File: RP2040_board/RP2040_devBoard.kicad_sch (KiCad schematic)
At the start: 14 parts, among them U1 RP2040

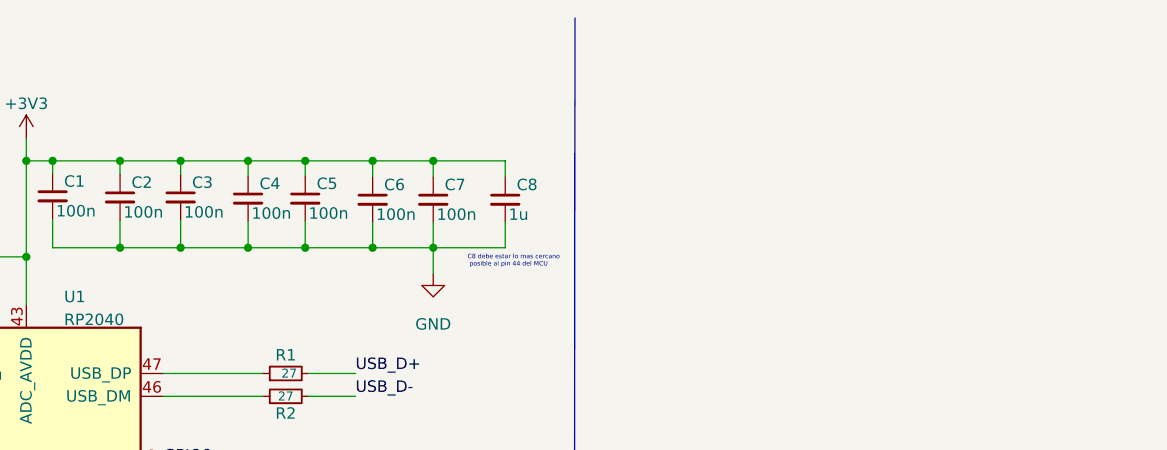
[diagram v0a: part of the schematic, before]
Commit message: ESCH: added the schematic of the power supply and did the wiring
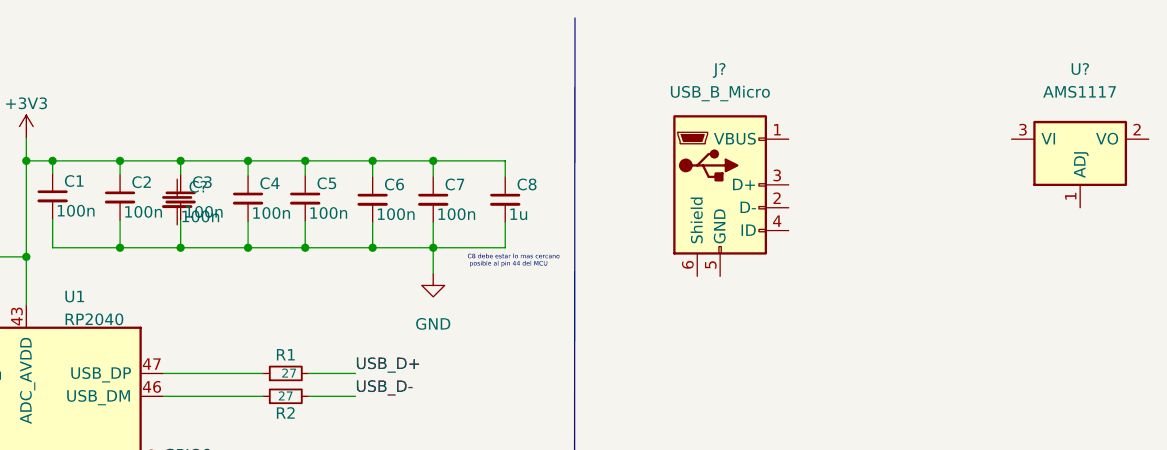
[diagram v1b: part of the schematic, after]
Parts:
- added C?: 100n, symbol Device:C_Small
- added J?: USB_B_Micro, symbol Connector:USB_B_Micro
- added U?: AMS1117, Package_TO_SOT_SMD:SOT-223-3_TabPin2, symbol Regulator_Linear:AMS1117
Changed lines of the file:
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@@
     (pin "2")
+  )
+  (symbol (lib_id "Connector:USB_B_Micro") (at 155.829 30.607 0) (unit 1)
+    (in_bom yes) (on_board yes) (fields_autoplaced)
+    (property "Reference" "J?" (id 0) (at 155.829 17.78 0))
+    (property "Value" "USB_B_Micro" (id 1) (at 155.829 20.32 0))
+    (property "Footprint" "" (id 2) (at 159.639 31.877 0)
+      (effects (font (size 1.27 1.27)) hide)
+    )
+    (property "Datasheet" "~" (id 3) (at 159.639 31.877 0)
+      (effects (font (size 1.27 1.27)) hide)
+    )
+    (pin "1")
+    (pin "2")
+    (pin "3")
+    (pin "4")
+    (pin "5")
+    (pin "6")
   )
   (symbol (lib_id "power:GND") (at 123.952 40.513 0) (unit 1)
@@
     (pin "1")
     (pin "2")
+  )
+  (symbol (lib_id "Device:C_Small") (at 95.504 32.512 0) (unit 1)
+    (in_bom yes) (on_board yes)
+    (property "Reference" "C?" (id 0) (at 96.774 30.861 0)
+      (effects (font (size 1.27 1.27)) (justify left))
+    )
+    (property "Value" "100n" (id 1) (at 95.885 34.163 0)
+      (effects (font (size 1.27 1.27)) (justify left))
+    )
+    (property "Footprint" "" (id 2) (at 95.504 32.512 0)
+      (effects (font (size 1.27 1.27)) hide)
+    )
+    (property "Datasheet" "~" (id 3) (at 95.504 32.512 0)
+      (effects (font (size 1.27 1.27)) hide)
+    )
+    (pin "1")
+    (pin "2")
+  )
+  (symbol (lib_id "Regulator_Linear:AMS1117") (at 195.834 25.527 0) (unit 1)
+    (in_bom yes) (on_board yes) (fields_autoplaced)
+    (property "Reference" "U?" (id 0) (at 195.834 17.78 0))
+    (property "Value" "AMS1117" (id 1) (at 195.834 20.32 0))
+    (property "Footprint" "Package_TO_SOT_SMD:SOT-223-3_TabPin2" (id 2) (at 195.834 20.447 0)
+      (effects (font (size 1.27 1.27)) hide)
+    )
+    (property "Datasheet" "http://www.advanced-monolithic.com/pdf/ds1117.pdf" (id 3) (at 198.374 31.877 0)
+      (effects (font (size 1.27 1.27)) hide)
+    )
+    (pin "1")
+    (pin "2")
+    (pin "3")
   )
   (symbol (lib_id "Device:C_Small") (at 117.221 32.258 0) (unit 1)
@@
       (reference "C11") (unit 1) (value "100n") (footprint "")
     )
+    (path "/c184ec07-2ca3-431a-b1d7-87c5d244f97c"
+      (reference "C?") (unit 1) (value "100n") (footprint "")
+    )
+    (path "/62979524-2b61-4177-baa6-d541cfcb37b3"
+      (reference "J?") (unit 1) (value "USB_B_Micro") (footprint "")
+    )
     (path "/ff75c5c2-f457-45cc-a1b3-0ec8763f2644"
       (reference "R1") (unit 1) (value "27 ") (footprint "")
@@
       (reference "U1") (unit 1) (value "RP2040") (footprint "RP2040_minimal:RP2040-QFN-56")
     )
-  )
+    (path "/c332c69c-d979-473f-ae67-7a4fc27098e4"
+      (reference "U?") (unit 1) (value "AMS1117") (footprint "Package_TO_SOT_SMD:SOT-223-3_TabPin2")
+    )
+  )

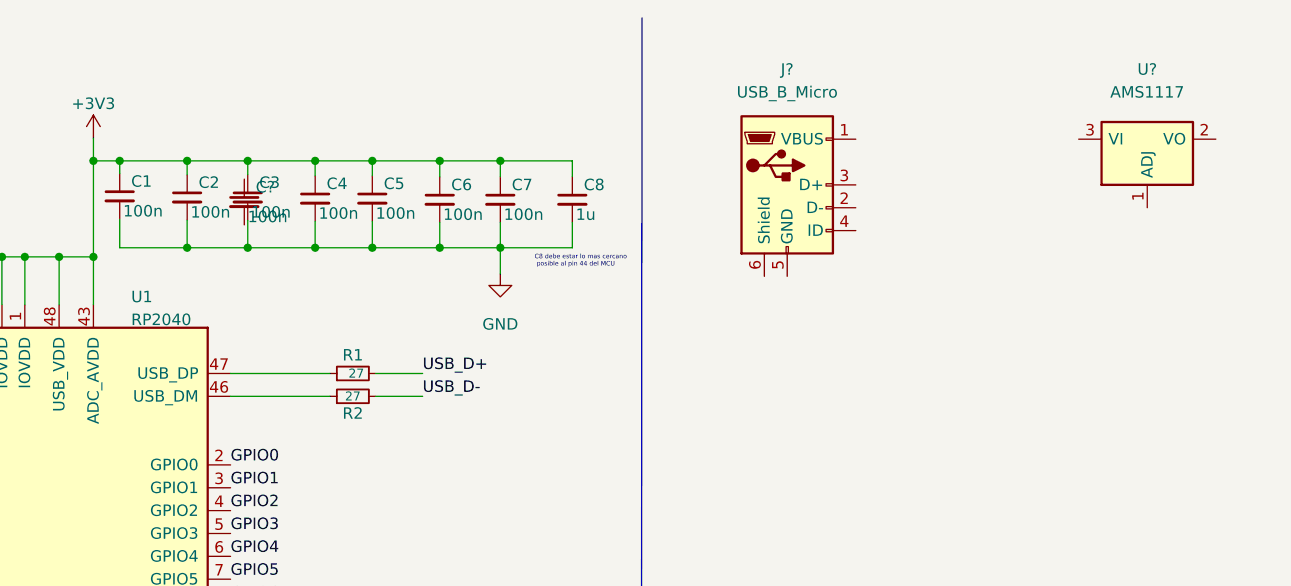
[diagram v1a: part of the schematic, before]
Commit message: sch: labeling of capacitor decoupling
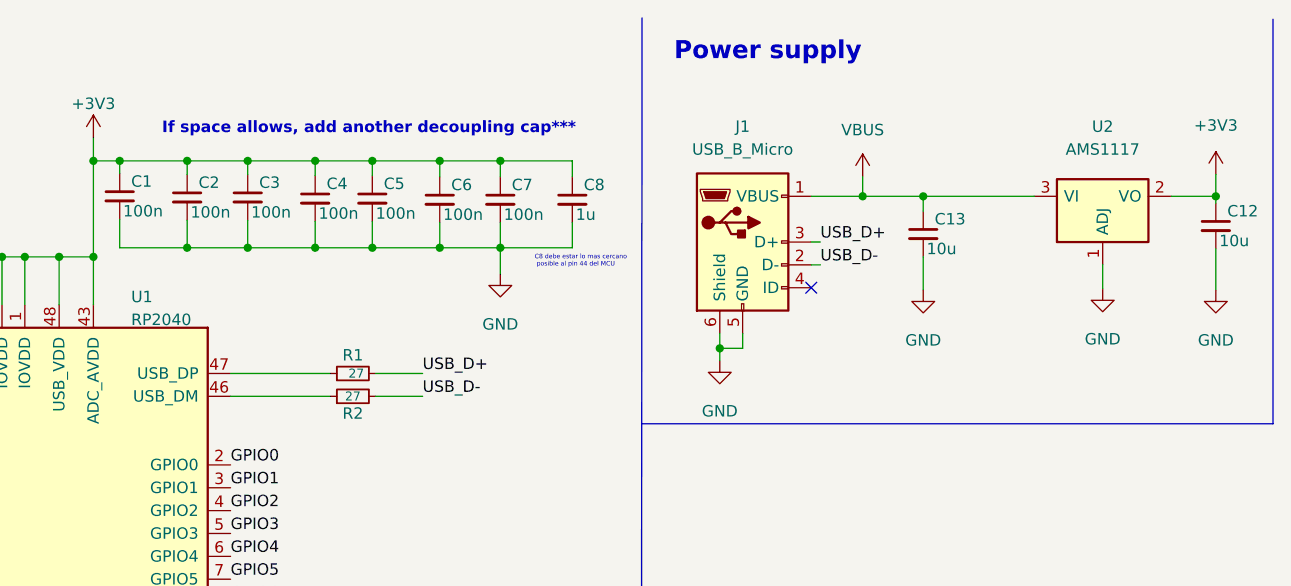
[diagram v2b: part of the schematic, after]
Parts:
- added C12: 10u, symbol Device:C_Small
- C13: renamed from C?; value 100n -> 10u
- gave numbers to parts that had none: 2
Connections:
- net +3V3: now also U2.2 (VO), C12.1
- net GND: now also C13.2, J1.5 (GND), J1.6 (Shield), U2.1 (ADJ), C12.2
- net USB_D+: now also J1.3 (D+)
- net USB_D-: now also J1.2 (D-)
- net VBUS: now reaches J1.1 (VBUS)
- net VBUS: now also C13.1, U2.3 (VI)
- no-connect marks 0 -> 1
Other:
- note added: "If space allows, add another decoupling cap***"
- note added: "Power supply"
- moved on the sheet: C13, J1, U2

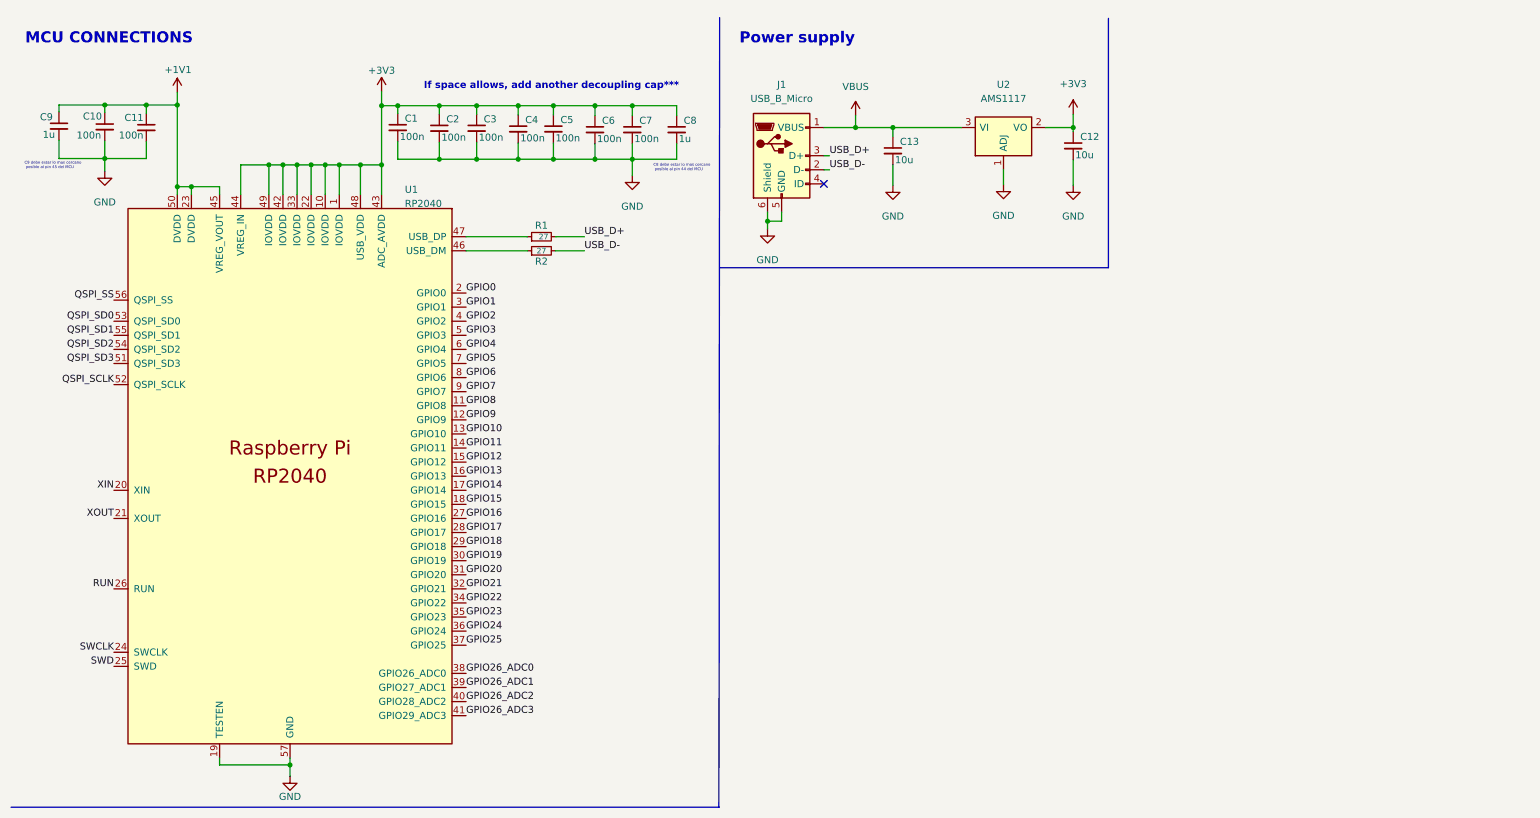
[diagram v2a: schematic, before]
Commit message: SCH: added the flash memory along with the push button, wiring included.
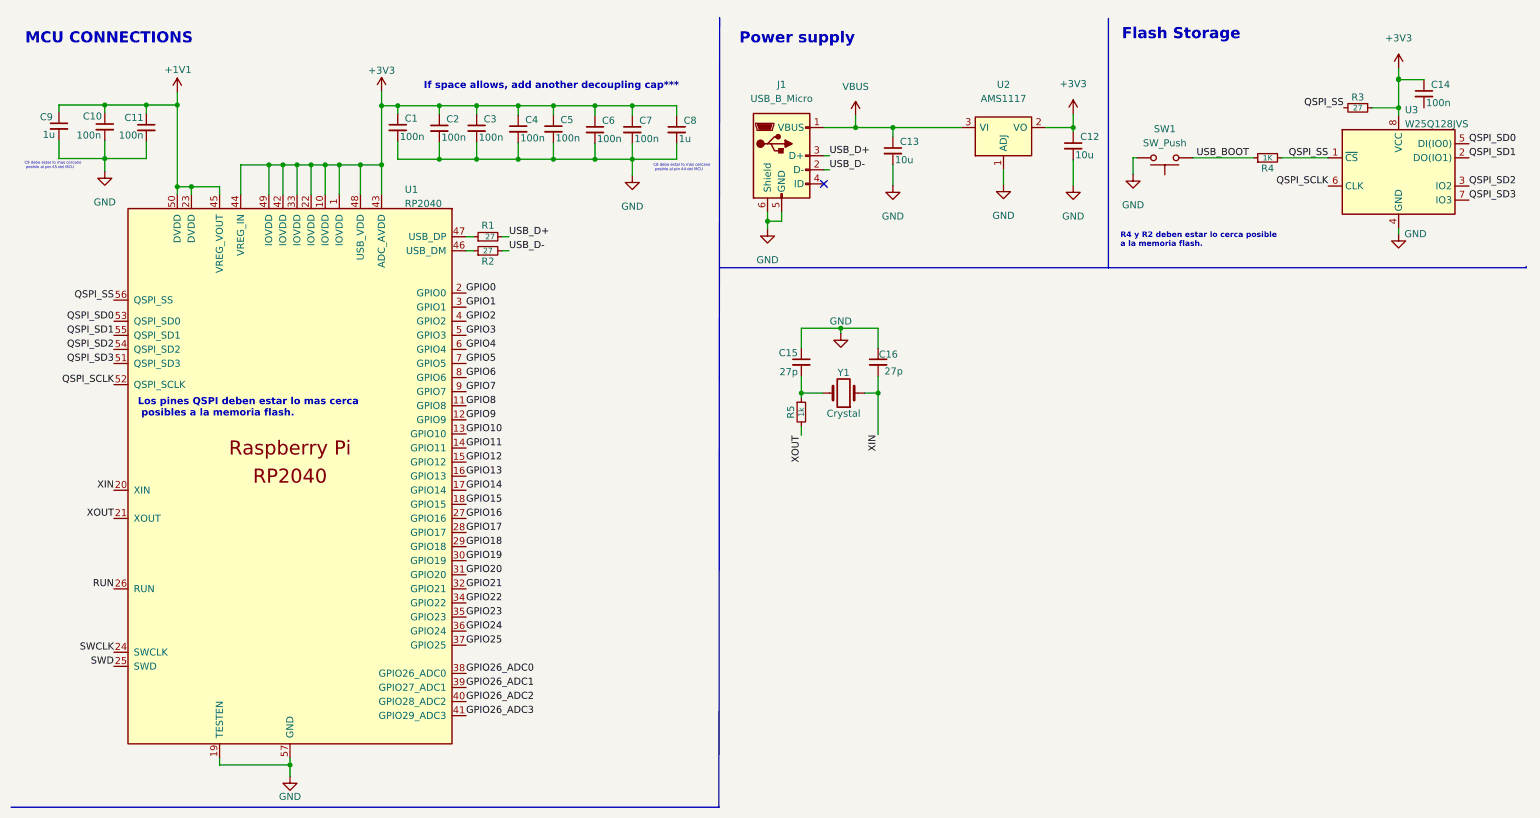
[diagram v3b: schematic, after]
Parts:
- added C14: 100n, symbol Device:C_Small
- added C15, C16: 27p, symbol Device:C_Small
- added R3: 27, symbol Device:R_Small
- added R4: 1K, symbol Device:R_Small
- added R5: 1k, symbol Device:R_Small
- added SW1: SW_Push, symbol Switch:SW_Push
- added U3: W25Q128JVS, Package_SO:SOIC-8_5.23x5.23mm_P1.27mm, symbol Memory_Flash:W25Q128JVS
- added Y1: Crystal, symbol Device:Crystal
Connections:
- net GND: now also C15.1, C16.1, SW1.1, U3.4 (GND)
- net QSPI_SCLK: now also U3.6 (CLK)
- net QSPI_SD0: now also U3.5 (DI(IO0))
- net QSPI_SD1: now also U3.2 (DO(IO1))
- net QSPI_SD2: now also U3.3 (IO2)
- net QSPI_SD3: now also U3.7 (IO3)
- net QSPI_SS: now also R3.2, R4.2, U3.1 (~{CS})
- net XIN: now also C16.2, Y1.1
- net XOUT: now also R5.2
- new net: C14.1, R3.1, U3.8 (VCC)
- new net: C15.2, R5.1, Y1.2
- new net USB_BOOT: R4.1, SW1.2
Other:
- note added: "Flash Storage"
- note added: "Los pines QSPI deben estar lo mas cerca posibles a la memoria flash."
- note added: "R4 y R2 deben estar lo cerca posible a la memoria flash."
- moved on the sheet: R1, R2

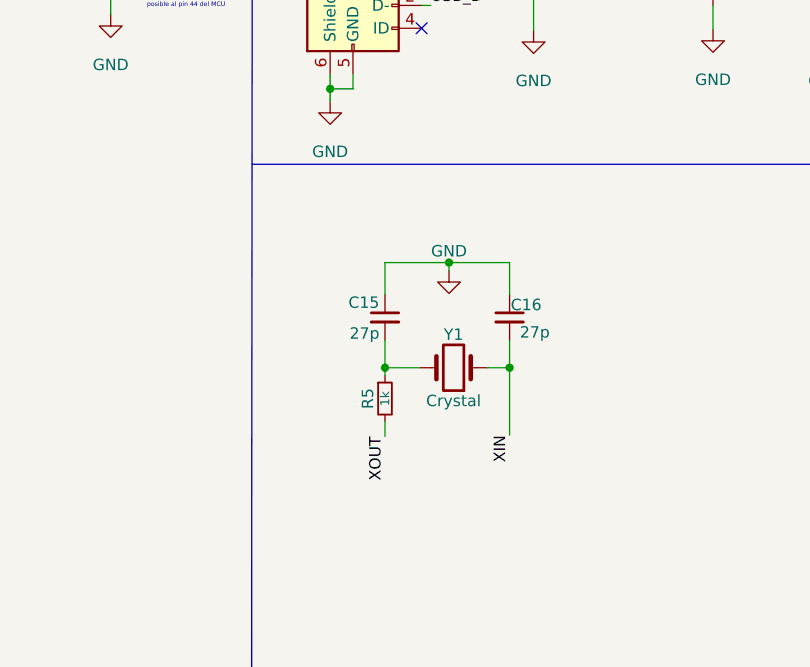
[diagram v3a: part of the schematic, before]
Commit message: sch:ful wiring of the crystal.
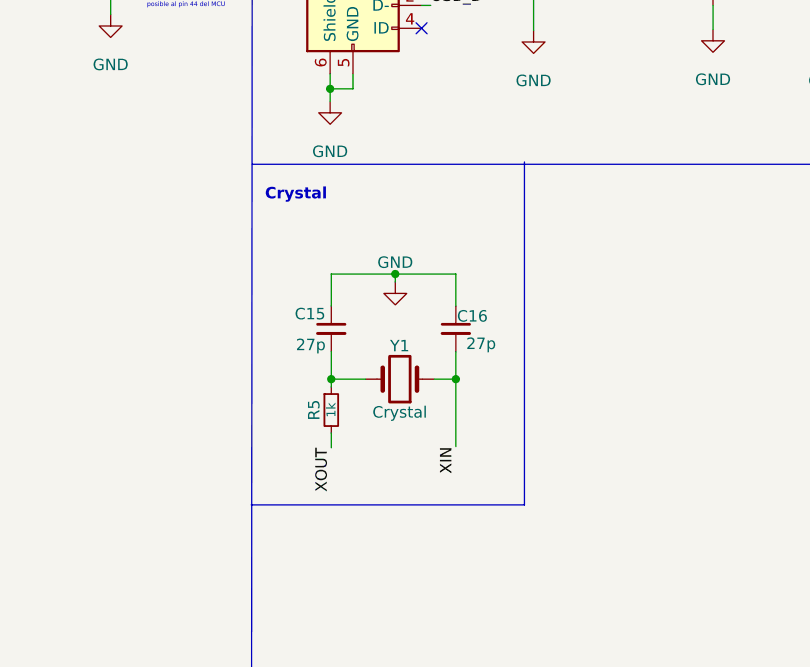
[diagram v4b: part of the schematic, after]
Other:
- note added: "Crystal"
- moved on the sheet: C15, C16, R5, Y1
